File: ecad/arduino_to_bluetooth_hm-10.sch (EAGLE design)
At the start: 2 parts

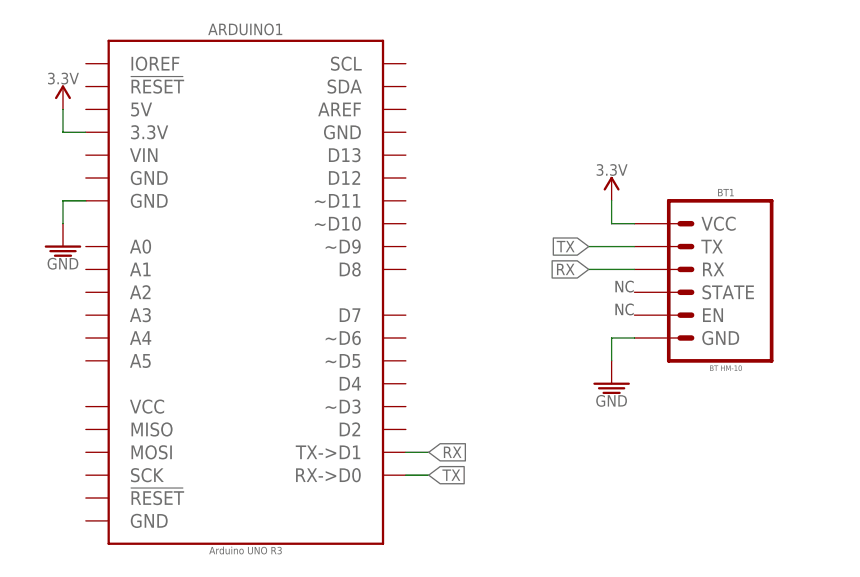
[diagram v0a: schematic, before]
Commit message: Update schematic, picture, and code
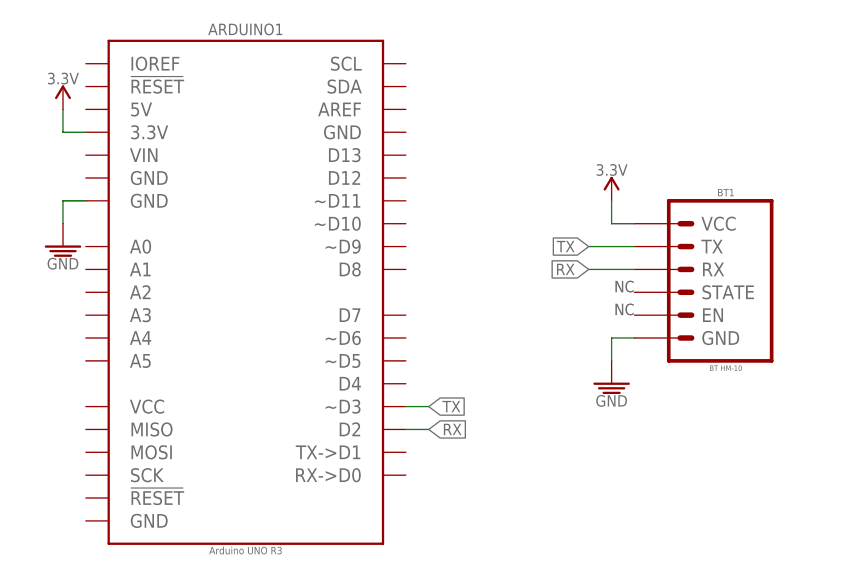
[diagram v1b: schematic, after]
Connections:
- net RX: now also ARDUINO1.D2; no longer ARDUINO1.TX->D1
- net TX: now also ARDUINO1.~D3; no longer ARDUINO1.RX->D0
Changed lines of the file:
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@@
 <net name="RX" class="0">
-<segment>
-<pinref part="ARDUINO1" gate="G$1" pin="TX-&gt;D1"/>
-<wire x1="66.04" y1="33.02" x2="68.58" y2="33.02" width="0.1524" layer="91"/>
-<label x="68.58" y="33.02" size="1.27" layer="95" ratio="10" xref="yes"/>
-</segment>
 <segment>
 <pinref part="BT1" gate="G$1" pin="RX"/>
@@
 <label x="86.36" y="53.34" size="1.27" layer="95" ratio="10" rot="R180" xref="yes"/>
 </segment>
+<segment>
+<pinref part="ARDUINO1" gate="G$1" pin="D2"/>
+<wire x1="68.58" y1="35.56" x2="66.04" y2="35.56" width="0.1524" layer="91"/>
+<label x="68.58" y="35.56" size="1.27" layer="95" ratio="10" xref="yes"/>
+</segment>
 </net>
 <net name="TX" class="0">
-<segment>
-<pinref part="ARDUINO1" gate="G$1" pin="RX-&gt;D0"/>
-<wire x1="68.58" y1="30.48" x2="66.04" y2="30.48" width="0.1524" layer="91"/>
-<label x="68.58" y="30.48" size="1.27" layer="95" ratio="10" xref="yes"/>
-</segment>
 <segment>
 <pinref part="BT1" gate="G$1" pin="TX"/>
@@
 <label x="86.36" y="55.88" size="1.27" layer="95" ratio="10" rot="R180" xref="yes"/>
 </segment>
+<segment>
+<pinref part="ARDUINO1" gate="G$1" pin="~D3"/>
+<wire x1="68.58" y1="38.1" x2="66.04" y2="38.1" width="0.1524" layer="91"/>
+<label x="68.58" y="38.1" size="1.27" layer="95" ratio="10" xref="yes"/>
+</segment>
 </net>

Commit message: Modify schematic to have voltage divider for BT HM-10
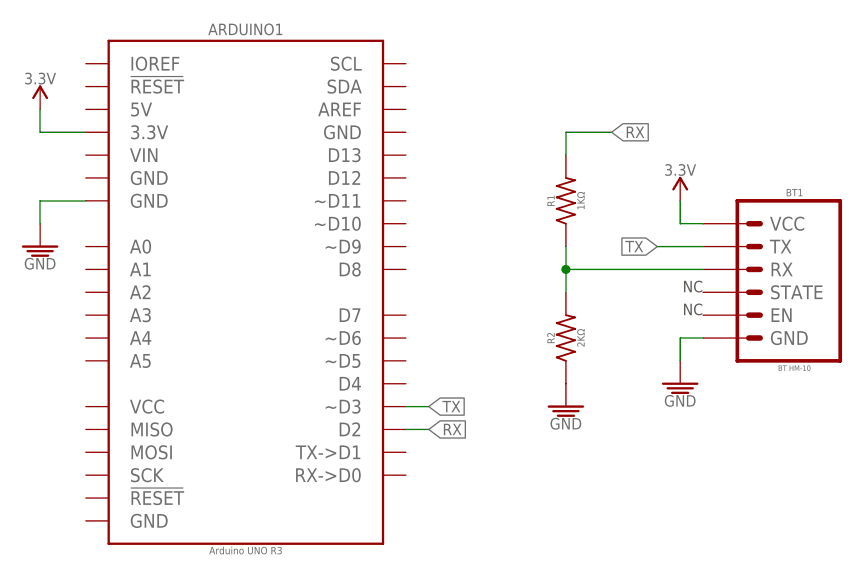
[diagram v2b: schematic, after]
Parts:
- added R1: 1KΩ, PiB_resistors:1KΩ_PTH-0207/7_1/8W-5%
- added R2: 2KΩ, PiB_resistors:2KΩ_PTH-0207/7_1/8W-5%
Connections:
- net GND: now also R2.1
- net RX: now also R1.1, R1.2, R2.2
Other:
- moved on the sheet: BT1
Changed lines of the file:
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@@
 <part name="SUPPLY3" library="PiB_power_symbols" deviceset="3.3V" device=""/>
 <part name="SUPPLY4" library="PiB_power_symbols" deviceset="3.3V" device=""/>
+<part name="R1" library="PiB_resistors" deviceset="1KΩ" device="_PTH-0207/7_1/8W-5%" value="1KΩ"/>
+<part name="R2" library="PiB_resistors" deviceset="2KΩ" device="_PTH-0207/7_1/8W-5%" value="2KΩ"/>
+<part name="SUPPLY5" library="PiB_power_symbols" deviceset="GND" device=""/>
 </parts>
 <sheets>
@@
 <instances>
 <instance part="ARDUINO1" gate="G$1" x="48.26" y="50.8"/>
-<instance part="BT1" gate="G$1" x="101.6" y="53.34" rot="MR0"/>
-<instance part="SUPPLY1" gate="GND" x="27.94" y="55.88"/>
-<instance part="SUPPLY2" gate="GND" x="88.9" y="40.64"/>
-<instance part="SUPPLY3" gate="3.3V" x="88.9" y="60.96"/>
-<instance part="SUPPLY4" gate="3.3V" x="27.94" y="71.12"/>
+<instance part="BT1" gate="G$1" x="109.22" y="53.34" rot="MR0"/>
+<instance part="SUPPLY1" gate="GND" x="25.4" y="55.88"/>
+<instance part="SUPPLY2" gate="GND" x="96.52" y="40.64"/>
+<instance part="SUPPLY3" gate="3.3V" x="96.52" y="60.96"/>
+<instance part="SUPPLY4" gate="3.3V" x="25.4" y="71.12"/>
+<instance part="R1" gate="G$1" x="83.82" y="60.96" rot="R90"/>
+<instance part="R2" gate="G$1" x="83.82" y="45.72" rot="R90"/>
+<instance part="SUPPLY5" gate="GND" x="83.82" y="38.1"/>
 </instances>
 <busses>
@@
 <segment>
 <pinref part="BT1" gate="G$1" pin="RX"/>
-<wire x1="91.44" y1="53.34" x2="86.36" y2="53.34" width="0.1524" layer="91"/>
-<label x="86.36" y="53.34" size="1.27" layer="95" ratio="10" rot="R180" xref="yes"/>
+<wire x1="99.06" y1="53.34" x2="83.82" y2="53.34" width="0.1524" layer="91"/>
+<pinref part="R2" gate="G$1" pin="2"/>
+<wire x1="83.82" y1="50.8" x2="83.82" y2="53.34" width="0.1524" layer="91"/>
+<junction x="83.82" y="53.34"/>
+<pinref part="R1" gate="G$1" pin="1"/>
+<wire x1="83.82" y1="55.88" x2="83.82" y2="53.34" width="0.1524" layer="91"/>
 </segment>
 <segment>
@@
 <label x="68.58" y="35.56" size="1.27" layer="95" ratio="10" xref="yes"/>
 </segment>
+<segment>
+<pinref part="R1" gate="G$1" pin="2"/>
+<wire x1="83.82" y1="66.04" x2="83.82" y2="68.58" width="0.1524" layer="91"/>
+<wire x1="83.82" y1="68.58" x2="88.9" y2="68.58" width="0.1524" layer="91"/>
+<label x="88.9" y="68.58" size="1.27" layer="95" ratio="10" xref="yes"/>
+</segment>
 </net>
 <net name="TX" class="0">
 <segment>
 <pinref part="BT1" gate="G$1" pin="TX"/>
-<wire x1="91.44" y1="55.88" x2="86.36" y2="55.88" width="0.1524" layer="91"/>
-<label x="86.36" y="55.88" size="1.27" layer="95" ratio="10" rot="R180" xref="yes"/>
+<wire x1="99.06" y1="55.88" x2="93.98" y2="55.88" width="0.1524" layer="91"/>
+<label x="93.98" y="55.88" size="1.27" layer="95" ratio="10" rot="R180" xref="yes"/>
 </segment>
 <segment>
@@
 <segment>
 <pinref part="ARDUINO1" gate="G$1" pin="GND@1"/>
-<wire x1="30.48" y1="60.96" x2="27.94" y2="60.96" width="0.1524" layer="91"/>
-<wire x1="27.94" y1="60.96" x2="27.94" y2="58.42" width="0.1524" layer="91"/>
+<wire x1="30.48" y1="60.96" x2="25.4" y2="60.96" width="0.1524" layer="91"/>
+<wire x1="25.4" y1="60.96" x2="25.4" y2="58.42" width="0.1524" layer="91"/>
 <pinref part="SUPPLY1" gate="GND" pin="GND"/>
 </segment>
 <segment>
 <pinref part="BT1" gate="G$1" pin="GND"/>
-<wire x1="91.44" y1="45.72" x2="88.9" y2="45.72" width="0.1524" layer="91"/>
-<wire x1="88.9" y1="45.72" x2="88.9" y2="43.18" width="0.1524" layer="91"/>
+<wire x1="99.06" y1="45.72" x2="96.52" y2="45.72" width="0.1524" layer="91"/>
+<wire x1="96.52" y1="45.72" x2="96.52" y2="43.18" width="0.1524" layer="91"/>
 <pinref part="SUPPLY2" gate="GND" pin="GND"/>
+</segment>
+<segment>
+<pinref part="R2" gate="G$1" pin="1"/>
+<pinref part="SUPPLY5" gate="GND" pin="GND"/>
 </segment>
 </net>
@@
 <segment>
 <pinref part="BT1" gate="G$1" pin="VCC"/>
-<wire x1="91.44" y1="58.42" x2="88.9" y2="58.42" width="0.1524" layer="91"/>
-<wire x1="88.9" y1="58.42" x2="88.9" y2="60.96" width="0.1524" layer="91"/>
+<wire x1="99.06" y1="58.42" x2="96.52" y2="58.42" width="0.1524" layer="91"/>
+<wire x1="96.52" y1="58.42" x2="96.52" y2="60.96" width="0.1524" layer="91"/>
 <pinref part="SUPPLY3" gate="3.3V" pin="3.3V"/>
 </segment>
 <segment>
 <pinref part="ARDUINO1" gate="G$1" pin="3.3V"/>
-<wire x1="30.48" y1="68.58" x2="27.94" y2="68.58" width="0.1524" layer="91"/>
-<wire x1="27.94" y1="68.58" x2="27.94" y2="71.12" width="0.1524" layer="91"/>
+<wire x1="30.48" y1="68.58" x2="25.4" y2="68.58" width="0.1524" layer="91"/>
+<wire x1="25.4" y1="68.58" x2="25.4" y2="71.12" width="0.1524" layer="91"/>
 <pinref part="SUPPLY4" gate="3.3V" pin="3.3V"/>
 </segment>

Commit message: Updated schematic with parts that reflect the appropriate parts list.  Updated picture to have resistor values without the ohm symbol
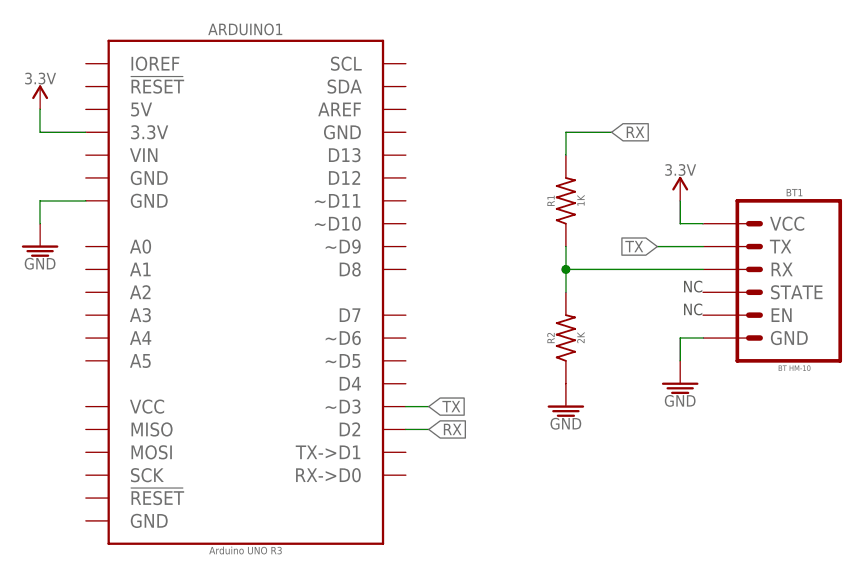
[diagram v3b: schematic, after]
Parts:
- R1: value 1KΩ -> 1K; device PiB_resistors:1KΩ_PTH-0207/7_1/8W-5% -> PiB_resistors:1KΩ_PTH-0207/7_1/4W-5%
- R2: value 2KΩ -> 2K; device PiB_resistors:2KΩ_PTH-0207/7_1/8W-5% -> PiB_resistors:2KΩ_PTH-0207/7_1/4W-5%
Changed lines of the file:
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@@
 <part name="SUPPLY3" library="PiB_power_symbols" deviceset="3.3V" device=""/>
 <part name="SUPPLY4" library="PiB_power_symbols" deviceset="3.3V" device=""/>
-<part name="R1" library="PiB_resistors" deviceset="1KΩ" device="_PTH-0207/7_1/8W-5%" value="1KΩ"/>
-<part name="R2" library="PiB_resistors" deviceset="2KΩ" device="_PTH-0207/7_1/8W-5%" value="2KΩ"/>
+<part name="R1" library="PiB_resistors" deviceset="1KΩ" device="_PTH-0207/7_1/4W-5%" value="1K"/>
+<part name="R2" library="PiB_resistors" deviceset="2KΩ" device="_PTH-0207/7_1/4W-5%" value="2K"/>
 <part name="SUPPLY5" library="PiB_power_symbols" deviceset="GND" device=""/>
 </parts>

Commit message: Fix mistake in code where the pin connections were discribed incorrectly.  Change schematic to be more clear.
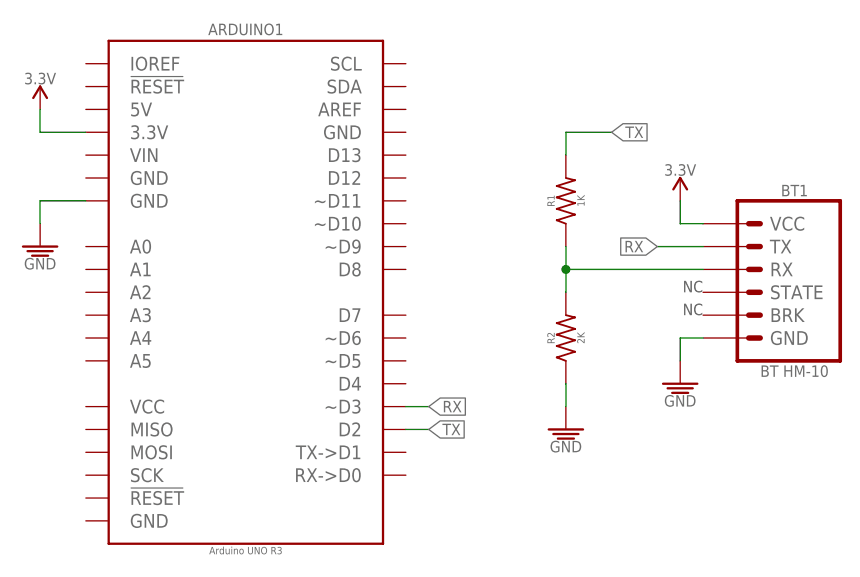
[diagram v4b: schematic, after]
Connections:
- net RX: now also ARDUINO1.~D3, BT1.TX; no longer ARDUINO1.D2, R1.2
- net TX: now also ARDUINO1.D2, R1.2; no longer ARDUINO1.~D3, BT1.TX
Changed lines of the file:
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@@
 <?xml version="1.0" encoding="utf-8"?>
 <!DOCTYPE eagle SYSTEM "eagle.dtd">
-<eagle version="8.6.3">
+<eagle version="9.0.1">
 <drawing>
 <settings>
@@
 <setting verticaltext="up"/>
 </settings>
-<grid distance="0.1" unitdist="inch" unit="inch" style="lines" multiple="1" display="no" altdistance="0.01" altunitdist="inch" altunit="inch"/>
+<grid distance="0.1" unitdist="inch" unit="inch" style="lines" multiple="1" display="no" altdistance="0.5" altunitdist="inch" altunit="inch"/>
 <layers>
 <layer number="1" name="Top" color="4" fill="1" visible="no" active="no"/>
@@
 <part name="SUPPLY3" library="PiB_power_symbols" deviceset="3.3V" device=""/>
 <part name="SUPPLY4" library="PiB_power_symbols" deviceset="3.3V" device=""/>
-<part name="R1" library="PiB_resistors" deviceset="1KΩ" device="_PTH-0207/7_1/4W-5%" value="1K"/>
-<part name="R2" library="PiB_resistors" deviceset="2KΩ" device="_PTH-0207/7_1/4W-5%" value="2K"/>
+<part name="R1" library="PiB_resistors" deviceset="1KΩ" device="_PTH-0207/7_1/4W-5%" package3d_urn="urn:adsk.eagle:package:2749854/2" value="1K"/>
+<part name="R2" library="PiB_resistors" deviceset="2KΩ" device="_PTH-0207/7_1/4W-5%" package3d_urn="urn:adsk.eagle:package:2749854/2" value="2K"/>
 <part name="SUPPLY5" library="PiB_power_symbols" deviceset="GND" device=""/>
 </parts>
@@
 <instance part="R1" gate="G$1" x="83.82" y="60.96" rot="R90"/>
 <instance part="R2" gate="G$1" x="83.82" y="45.72" rot="R90"/>
-<instance part="SUPPLY5" gate="GND" x="83.82" y="38.1"/>
+<instance part="SUPPLY5" gate="GND" x="83.82" y="35.56"/>
 </instances>
 <busses>
@@
 </segment>
 <segment>
-<pinref part="ARDUINO1" gate="G$1" pin="D2"/>
-<wire x1="68.58" y1="35.56" x2="66.04" y2="35.56" width="0.1524" layer="91"/>
-<label x="68.58" y="35.56" size="1.27" layer="95" ratio="10" xref="yes"/>
-</segment>
+<pinref part="ARDUINO1" gate="G$1" pin="~D3"/>
+<wire x1="68.58" y1="38.1" x2="66.04" y2="38.1" width="0.1524" layer="91"/>
+<label x="68.58" y="38.1" size="1.27" layer="95" ratio="10" xref="yes"/>
+</segment>
+<segment>
+<pinref part="BT1" gate="G$1" pin="TX"/>
+<wire x1="99.06" y1="55.88" x2="93.98" y2="55.88" width="0.1524" layer="91"/>
+<label x="93.98" y="55.88" size="1.27" layer="95" ratio="10" rot="R180" xref="yes"/>
+</segment>
+</net>
+<net name="GND" class="0">
+<segment>
+<pinref part="ARDUINO1" gate="G$1" pin="GND@1"/>
+<wire x1="30.48" y1="60.96" x2="25.4" y2="60.96" width="0.1524" layer="91"/>
+<wire x1="25.4" y1="60.96" x2="25.4" y2="58.42" width="0.1524" layer="91"/>
+<pinref part="SUPPLY1" gate="GND" pin="GND"/>
+</segment>
+<segment>
+<pinref part="BT1" gate="G$1" pin="GND"/>
+<wire x1="99.06" y1="45.72" x2="96.52" y2="45.72" width="0.1524" layer="91"/>
+<wire x1="96.52" y1="45.72" x2="96.52" y2="43.18" width="0.1524" layer="91"/>
+<pinref part="SUPPLY2" gate="GND" pin="GND"/>
+</segment>
+<segment>
+<pinref part="R2" gate="G$1" pin="1"/>
+<pinref part="SUPPLY5" gate="GND" pin="GND"/>
+<wire x1="83.82" y1="38.1" x2="83.82" y2="40.64" width="0.1524" layer="91"/>
+</segment>
+</net>
+<net name="3.3V" class="0">
+<segment>
+<pinref part="BT1" gate="G$1" pin="VCC"/>
+<wire x1="99.06" y1="58.42" x2="96.52" y2="58.42" width="0.1524" layer="91"/>
+<wire x1="96.52" y1="58.42" x2="96.52" y2="60.96" width="0.1524" layer="91"/>
+<pinref part="SUPPLY3" gate="3.3V" pin="3.3V"/>
+</segment>
+<segment>
+<pinref part="ARDUINO1" gate="G$1" pin="3.3V"/>
+<wire x1="30.48" y1="68.58" x2="25.4" y2="68.58" width="0.1524" layer="91"/>
+<wire x1="25.4" y1="68.58" x2="25.4" y2="71.12" width="0.1524" layer="91"/>
+<pinref part="SUPPLY4" gate="3.3V" pin="3.3V"/>
+</segment>
+</net>
+<net name="TX" class="0">
 <segment>
 <pinref part="R1" gate="G$1" pin="2"/>
@@
 <label x="88.9" y="68.58" size="1.27" layer="95" ratio="10" xref="yes"/>
 </segment>
-</net>
-<net name="TX" class="0">
-<segment>
-<pinref part="BT1" gate="G$1" pin="TX"/>
-<wire x1="99.06" y1="55.88" x2="93.98" y2="55.88" width="0.1524" layer="91"/>
-<label x="93.98" y="55.88" size="1.27" layer="95" ratio="10" rot="R180" xref="yes"/>
-</segment>
-<segment>
-<pinref part="ARDUINO1" gate="G$1" pin="~D3"/>
-<wire x1="68.58" y1="38.1" x2="66.04" y2="38.1" width="0.1524" layer="91"/>
-<label x="68.58" y="38.1" size="1.27" layer="95" ratio="10" xref="yes"/>
-</segment>
-</net>
-<net name="GND" class="0">
-<segment>
-<pinref part="ARDUINO1" gate="G$1" pin="GND@1"/>
-<wire x1="30.48" y1="60.96" x2="25.4" y2="60.96" width="0.1524" layer="91"/>
-<wire x1="25.4" y1="60.96" x2="25.4" y2="58.42" width="0.1524" layer="91"/>
-<pinref part="SUPPLY1" gate="GND" pin="GND"/>
-</segment>
-<segment>
-<pinref part="BT1" gate="G$1" pin="GND"/>
-<wire x1="99.06" y1="45.72" x2="96.52" y2="45.72" width="0.1524" layer="91"/>
-<wire x1="96.52" y1="45.72" x2="96.52" y2="43.18" width="0.1524" layer="91"/>
-<pinref part="SUPPLY2" gate="GND" pin="GND"/>
-</segment>
-<segment>
-<pinref part="R2" gate="G$1" pin="1"/>
-<pinref part="SUPPLY5" gate="GND" pin="GND"/>
-</segment>
-</net>
-<net name="3.3V" class="0">
-<segment>
-<pinref part="BT1" gate="G$1" pin="VCC"/>
-<wire x1="99.06" y1="58.42" x2="96.52" y2="58.42" width="0.1524" layer="91"/>
-<wire x1="96.52" y1="58.42" x2="96.52" y2="60.96" width="0.1524" layer="91"/>
-<pinref part="SUPPLY3" gate="3.3V" pin="3.3V"/>
-</segment>
-<segment>
-<pinref part="ARDUINO1" gate="G$1" pin="3.3V"/>
-<wire x1="30.48" y1="68.58" x2="25.4" y2="68.58" width="0.1524" layer="91"/>
-<wire x1="25.4" y1="68.58" x2="25.4" y2="71.12" width="0.1524" layer="91"/>
-<pinref part="SUPPLY4" gate="3.3V" pin="3.3V"/>
+<segment>
+<pinref part="ARDUINO1" gate="G$1" pin="D2"/>
+<wire x1="68.58" y1="35.56" x2="66.04" y2="35.56" width="0.1524" layer="91"/>
+<label x="68.58" y="35.56" size="1.27" layer="95" ratio="10" xref="yes"/>
 </segment>
 </net>
@@
 </schematic>
 </drawing>
+<compatibility>
+<note version="8.3" severity="warning">
+Since Version 8.3, EAGLE supports URNs for individual library
+assets (packages, symbols, and devices). The URNs of those assets
+will not be understood (or retained) with this version.
+</note>
+<note version="8.3" severity="warning">
+Since Version 8.3, EAGLE supports the association of 3D packages
+with devices in libraries, schematics, and board files. Those 3D
+packages will not be understood (or retained) with this version.
+</note>
+</compatibility>
 </eagle>
